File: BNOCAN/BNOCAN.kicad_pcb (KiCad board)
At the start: 2 copper layers, 50 x 50 mm, 56 parts, among them J1 CANConn, J2 PWRConn, J3 SWDConn, Q1 MMBT3904, Q2 MMBT3904, SW1 RST, U1 TPS560430X3FDBVR, U2 SN65HVD230, U4 STM32F103T8Ux, U5 BNO085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

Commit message: V1.1 Produced
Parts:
- removed C21: Super, Capacitor_THT:CP_Radial_D13.0mm_P5.00mm
- removed Q1, Q2: MMBT3904, Package_TO_SOT_SMD:SOT-23
- removed R1: 51k, Resistor_SMD:R_0603_1608Metric
- removed R18, R3: 100, Resistor_SMD:R_0402_1005Metric
- removed R2: 22.1k, Resistor_SMD:R_0603_1608Metric
- removed R6, R7, R8: 0, Resistor_SMD:R_0402_1005Metric
- added R17: 10k, Resistor_SMD:R_0603_1608Metric, F.Cu at (139.2, 87.7)
- SW1: value RST -> BOOT
- moved D3 7.27 mm to (135.8, 92.7)
- moved D1 7.18 mm to (132.7, 92.8)
- moved C14 6.74 mm to (124.8, 68.1)
- moved R4 5.70 mm to (135.3, 90.5), turned to 180 degrees
- moved R14 2.85 mm to (119.3, 67.5)
- moved R9 2.49 mm to (134.1, 76.5), turned to 90 degrees
- moved C11 1.92 mm to (127.9, 69.3), turned to 180 degrees
- moved C12 1.92 mm to (127.9, 64.1), turned to 180 degrees
- moved C9 1.64 mm to (135.1, 87.7), turned to 180 degrees
- moved C8 1.28 mm to (135.3, 85.9), turned to 180 degrees
- moved C18 0.73 mm to (140.8, 71.2)
- moved R10 0.50 mm to (145.0, 67.9)
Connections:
- C10 pad 1: Net-(U4-BOOT0) -> +3.3V
- C10 pad 2: GND -> Net-(U4-BOOT0)
- C14 pad 2: /~{RST} -> /~{NRST}
- J3 pad 12: /~{RST} -> /~{NRST}
- R14 pad 2: +3.3V -> GND
- R4 pad 2: Net-(Q2-E) -> Net-(U4-PA3)
- R5 pad 2: Net-(Q1-B) -> Net-(D1-A)
- SW1 pad 1: GND -> Net-(U4-BOOT0)
- SW1 pad 2: Net-(U4-BOOT0) -> +3.3V
- U1 pad 3: Net-(U1-FB) -> +3.3V
- U4 pad 11: unconnected-(U4-PA4-Pad11) -> /~{CS}
- U4 pad 20: unconnected-(U4-PA8-Pad20) -> /~{IMU_INTR}
- U4 pad 4: /~{RST} -> /~{NRST}
- U5 pad 11: /NRST -> /~{NRST}
- U5 pad 17: Net-(U5-H_SA0/MOSI) -> /MOSI
- U5 pad 18: unconnected-(U5-H_CSN-Pad18) -> /~{CS}
- U5 pad 19: Net-(U5-H_SCL/SCLK/RX) -> /SPICLK
- U5 pad 20: Net-(U5-H_SDA/MISO/TX) -> /MISO
- U5 pad 4: +3.3V -> Net-(U5-BOOTN)
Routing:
- net /~{NRST}: track 0.00 -> 76.5 mm, vias 0 -> 2
- net /~{RST}: track 40.3 -> 0.00 mm
- net +3.3V: track 201.1 -> 233.7 mm, vias 3 -> 6
- net /~{IMU_INTR}: track 0.00 -> 20.9 mm, vias 0 -> 2
- net /~{CS}: track 0.00 -> 13.8 mm, vias 0 -> 2
- net Net-(U5-H_SA0/MOSI): track 7.62 -> 0.00 mm
- net /MISO: track 4.89 -> 10.2 mm, vias 0 -> 2
- net /MOSI: track 1.24 -> 6.37 mm
- net Net-(U5-H_SDA/MISO/TX): track 5.10 -> 0.00 mm, vias 2 -> 0
- net Net-(U5-BOOTN): track 0.00 -> 4.45 mm
- net Net-(U1-FB): track 4.22 -> 0.00 mm
- net /SPICLK: track 4.82 -> 8.52 mm
- net Net-(U4-BOOT0): track 44.9 -> 48.2 mm
- net Net-(U5-H_SCL/SCLK/RX): track 2.73 -> 0.00 mm
- net Net-(D1-A): track 3.13 -> 1.51 mm
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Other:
- board text added: "BNOCAN V1.1 Raheel Rehmatullah January 2024"
- board text removed: "BNOCAN Raheel Rehmatullah December 2023"

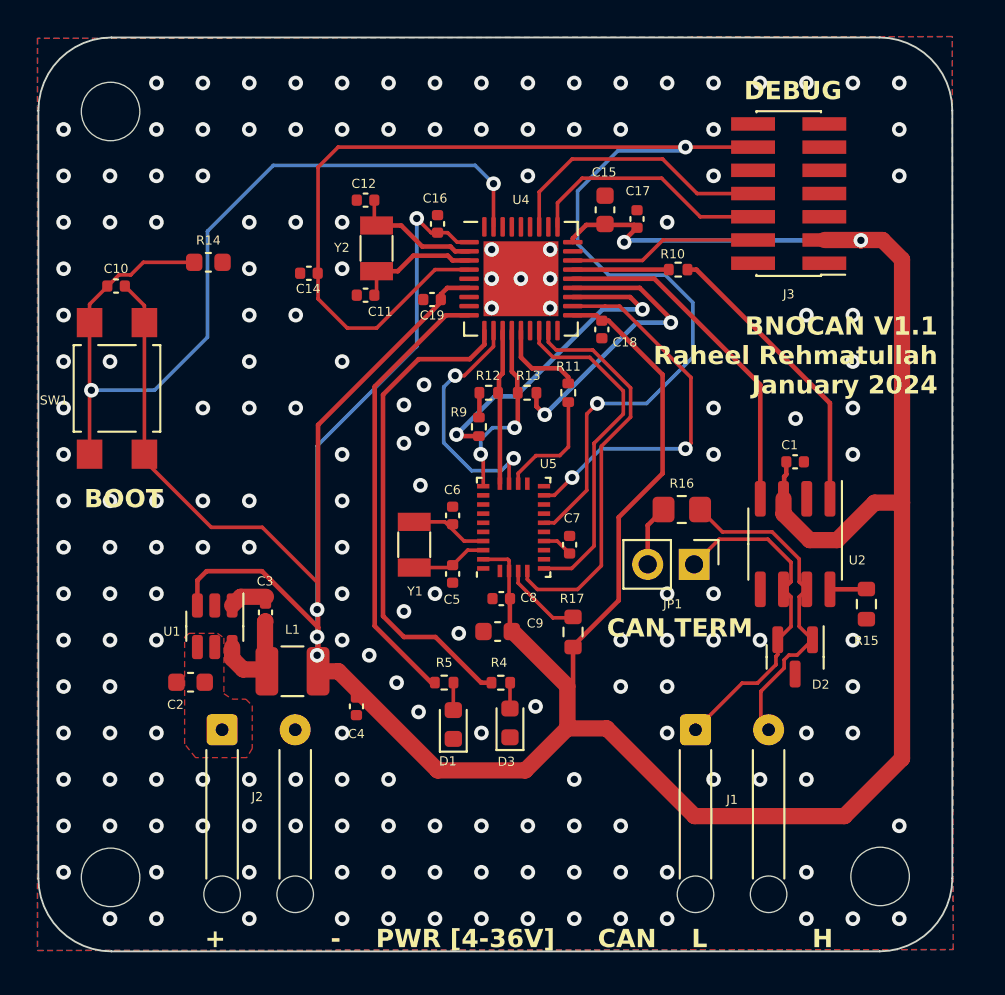
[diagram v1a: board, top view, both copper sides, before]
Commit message: Firmware Dump + some Board Bug fixes
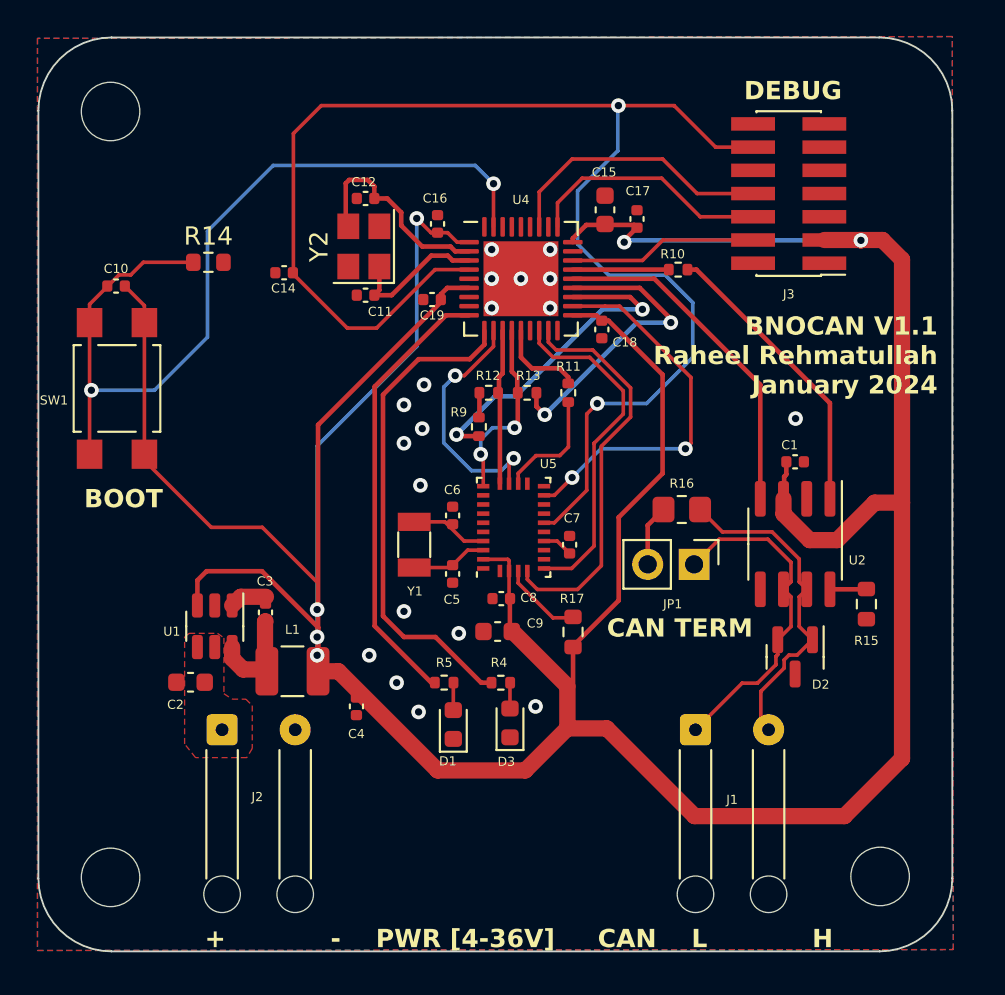
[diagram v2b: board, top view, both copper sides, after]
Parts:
- C11, C12: value 22pF -> 8pF
- R14: footprint Capacitor_SMD:C_0603_1608Metric -> Resistor_SMD:R_0603_1608Metric
- Y2: footprint Crystal:Crystal_SMD_3215-2Pin_3.2x1.5mm -> Crystal:Crystal_SMD_3225-4Pin_3.2x2.5mm
- moved C14 1.36 mm to (123.4, 68.1)
- moved Y2 0.70 mm to (127.8, 66.6)
- moved C12 0.09 mm to (127.9, 64.0)
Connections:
- Y2 pad 1: Net-(U4-PD0) -> Net-(U4-PD1)
- Y2 pad 2: Net-(U4-PD1) -> GND
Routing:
- net Net-(U4-PD0): track 7.08 -> 11.7 mm
- net /~{NRST}: track 76.5 -> 80.0 mm
- net Net-(U4-PD1): track 6.89 -> 8.04 mm
- net GND: track 0.00 -> 0.17 mm, vias 180 -> 19
